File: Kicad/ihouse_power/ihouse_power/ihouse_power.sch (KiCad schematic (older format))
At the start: 14 parts, among them J10 Conn_02x07_Odd_Even, J11 Conn_01x06, J12 Conn_01x06, J14 Optic, J15 Hum1, J16 Hum2, J17 Hum3, J18 Temp, J19 I2C, J5 Conn_01x16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

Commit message: schemos, pcb ruosimas
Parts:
- added M3: ev1527receiver_module, ev1527:EV1527_Receiver, symbol ev1527_receiver_module:ev1527receiver_module
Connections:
- wire segments 159 -> 167
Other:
- moved on the sheet: J10, J11, J12, J14, J15, J16, J17, J18, J19, J5, J6, J7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

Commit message: schemos ir pcb plokstes ruosimas
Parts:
- M3: symbol ev1527_receiver_module:ev1527receiver_module -> ihouse_power-rescue:ev1527receiver_module-ev1527_receiver_module
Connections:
- wire segments 167 -> 166
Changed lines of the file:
@@
 EESchema Schematic File Version 4
 LIBS:ihouse_power-cache
-EELAYER 26 0
+EELAYER 29 0
 EELAYER END
 $Descr A4 11693 8268
@@
 F32 "QCH_D2" O L 2750 1350 50
 F33 "QCH_D3" O L 2750 1250 50
+F34 "3VDC" O L 2750 1650 50
 $EndSheet
 Wire Wire Line
@@
 	4100 3400 4450 3400
 $Comp
-L ev1527_receiver_module:ev1527receiver_module M3
+L ihouse_power-rescue:ev1527receiver_module-ev1527_receiver_module M3
 U 1 1 5CAFFFFB
 P 1350 1450
@@
 Connection ~ 2300 2100
 Wire Wire Line
-	2400 1650 2400 1900
-Wire Wire Line
-	1650 1650 2400 1650
+	1650 1650 2750 1650
 Wire Bus Line
 	5550 950  5550 2050

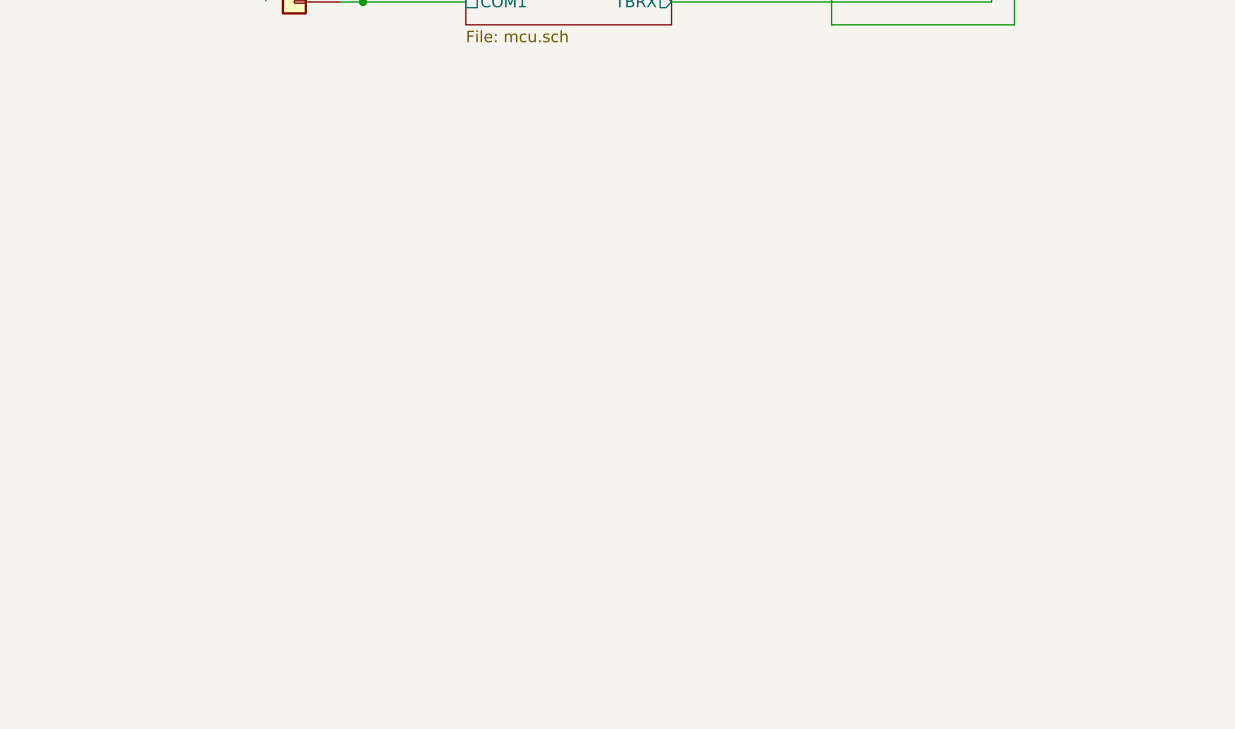
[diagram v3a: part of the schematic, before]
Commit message: prideta schema ir pcb lcd ekrano rs232 draiverio
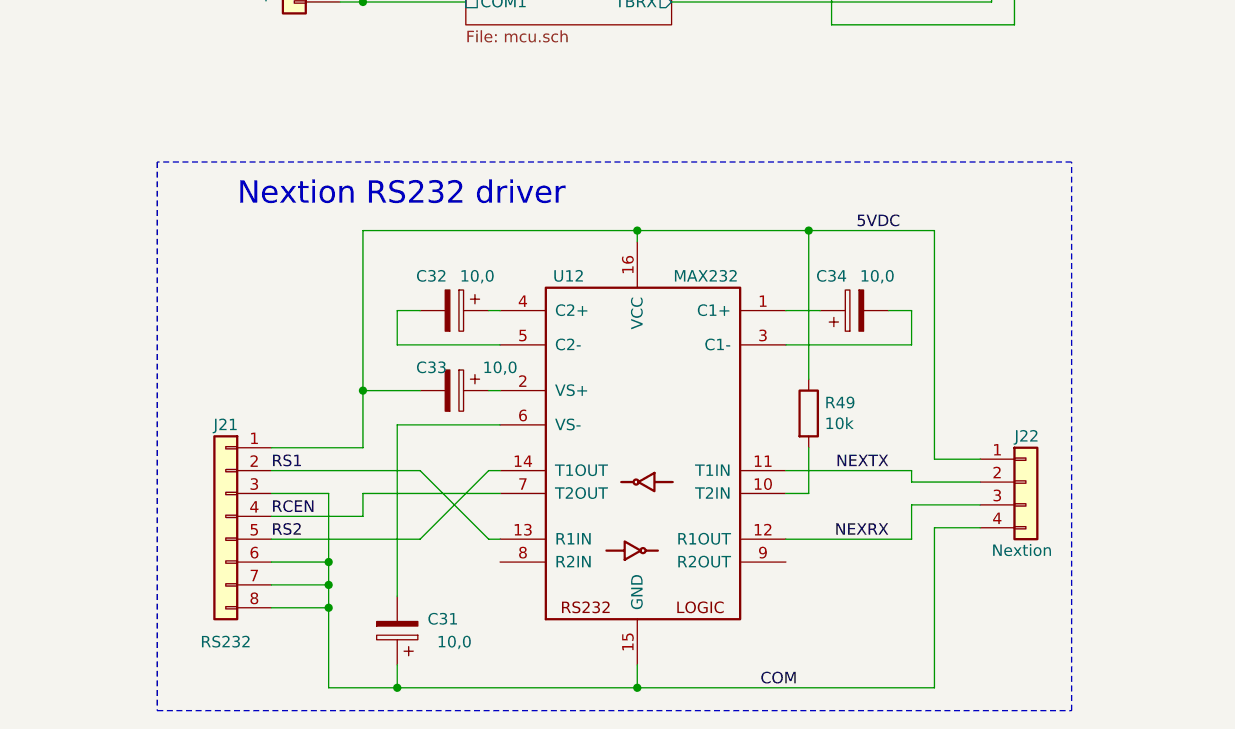
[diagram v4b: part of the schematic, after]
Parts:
- added C31, C32, C33, C34: 10,0, Capacitor_SMD:CP_Elec_3x5.4, symbol Device:CP
- added J21: RS232, Connector_PinHeader_2.54mm:PinHeader_1x08_P2.54mm_Horizontal, symbol Connector_Generic:Conn_01x08
- added J22: Nextion, Connector_PinHeader_2.54mm:PinHeader_1x04_P2.54mm_Vertical, symbol Connector_Generic:Conn_01x04
- added R49: 10k, symbol Device:R
- added U12: MAX232, Package_SO:SOIC-16_3.9x9.9mm_P1.27mm, symbol ihouse_power-rescue:MAX232-ics
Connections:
- new net: C34.1, U12.1 (C1+)
- new net: R49.2, U12.10 (T2IN)
- new net: C33.1, U12.2 (VS+)
- new net: C34.2, U12.3 (C1-)
- new net: C32.1, U12.4 (C2+)
- new net: C32.2, U12.5 (C2-)
- new net: C31.2, U12.6 (VS-)
- new net 5VDC: C33.2, J21.1 (Pin_1), J22.1 (Pin_1), R49.1, U12.16 (VCC)
- new net COM: C31.1, J21.3 (Pin_3), J21.6 (Pin_6), J21.7 (Pin_7), J21.8 (Pin_8), J22.4 (Pin_4), U12.15 (GND)
- new net NEXRX: J22.3 (Pin_3), U12.12 (R1OUT)
- new net NEXTX: J22.2 (Pin_2), U12.11 (T1IN)
- new net RCEN: J21.4 (Pin_4), U12.7 (T2OUT)
- new net RS1: J21.2 (Pin_2), U12.13 (R1IN)
- new net RS2: J21.5 (Pin_5), U12.14 (T1OUT)
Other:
- note added: "Nextion RS232 driver"
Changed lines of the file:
@@
 Wire Wire Line
 	1650 1650 2750 1650
+$Comp
+L ihouse_power-rescue:MAX232-ics U?
+U 1 1 5CF1CE1C
+P 3500 5900
+AR Path="/5D803411/5CF1CE1C" Ref="U?"  Part="1"
+AR Path="/5CF1CE1C" Ref="U12"  Part="1"
+F 0 "U12" H 3800 6700 50  0000 C CNN
+F 1 "MAX232" H 3200 6700 50  0000 C CNN
+F 2 "Package_SO:SOIC-16_3.9x9.9mm_P1.27mm" H 3550 4850 50  0001 L CNN
+F 3 "http://www.ti.com/lit/ds/symlink/max232.pdf" H 3500 5650 50  0001 C CNN
+	1    3500 5900
+	-1   0    0    -1
+$EndComp
+Wire Wire Line
+	3500 6800 3500 6900
+Text Label 4200 6900 2    50   ~ 0
+COM
+Wire Wire Line
+	2900 5250 2850 5250
+Wire Wire Line
+	2900 5400 2450 5400
+Wire Wire Line
+	2450 5400 2450 5250
+Wire Wire Line
+	2450 5250 2550 5250
+Wire Wire Line
+	4150 5250 4300 5250
+Wire Wire Line
+	4600 5250 4700 5250
+Wire Wire Line
+	4700 5250 4700 5400
+Wire Wire Line
+	4700 5400 4150 5400
+Wire Wire Line
+	2850 5600 2900 5600
+Wire Wire Line
+	3500 4900 2300 4900
+Wire Wire Line
+	2300 4900 2300 5600
+Wire Wire Line
+	3500 4900 3500 4950
+Wire Wire Line
+	2300 5600 2550 5600
+Wire Wire Line
+	2450 5750 2450 6500
+Wire Wire Line
+	2450 6800 2450 6900
+Wire Wire Line
+	2450 6900 3500 6900
+Connection ~ 3500 6900
+$Comp
+L Device:CP C?
+U 1 1 5CF1CE39
+P 2700 5250
+AR Path="/5D803411/5CF1CE39" Ref="C?"  Part="1"
+AR Path="/5CF1CE39" Ref="C32"  Part="1"
+F 0 "C32" V 2550 5150 50  0000 C CNN
+F 1 "10,0" V 2550 5350 50  0000 C CNN
+F 2 "Capacitor_SMD:CP_Elec_3x5.4" H 2738 5100 50  0001 C CNN
+F 3 "~" H 2700 5250 50  0001 C CNN
+	1    2700 5250
+	0    1    1    0
+$EndComp
+$Comp
+L Device:CP C?
+U 1 1 5CF1CE40
+P 4450 5250
+AR Path="/5D803411/5CF1CE40" Ref="C?"  Part="1"
+AR Path="/5CF1CE40" Ref="C34"  Part="1"
+F 0 "C34" V 4600 5350 50  0000 C CNN
+F 1 "10,0" V 4600 5150 50  0000 C CNN
+F 2 "Capacitor_SMD:CP_Elec_3x5.4" H 4488 5100 50  0001 C CNN
+F 3 "~" H 4450 5250 50  0001 C CNN
+	1    4450 5250
+	0    -1   -1   0
+$EndComp
+$Comp
+L Device:CP C?
+U 1 1 5CF1CE47
+P 2700 5600
+AR Path="/5D803411/5CF1CE47" Ref="C?"  Part="1"
+AR Path="/5CF1CE47" Ref="C33"  Part="1"
+F 0 "C33" V 2600 5500 50  0000 C CNN
+F 1 "10,0" V 2600 5800 50  0000 C CNN
+F 2 "Capacitor_SMD:CP_Elec_3x5.4" H 2738 5450 50  0001 C CNN
+F 3 "~" H 2700 5600 50  0001 C CNN
+	1    2700 5600
+	0    1    1    0
+$EndComp
+$Comp
+L Device:CP C?
+U 1 1 5CF1CE4E
+P 2450 6650
+AR Path="/5D803411/5CF1CE4E" Ref="C?"  Part="1"
+AR Path="/5CF1CE4E" Ref="C31"  Part="1"
+F 0 "C31" H 2250 6600 50  0000 C CNN
+F 1 "10,0" H 2200 6700 50  0000 C CNN
+F 2 "Capacitor_SMD:CP_Elec_3x5.4" H 2488 6500 50  0001 C CNN
+F 3 "~" H 2450 6650 50  0001 C CNN
+	1    2450 6650
+	-1   0    0    1
+$EndComp
+Wire Wire Line
+	2450 5750 2900 5750
+Wire Wire Line
+	1900 5850 2300 5850
+Wire Wire Line
+	2300 5850 2300 5600
+Connection ~ 2300 5600
+Wire Wire Line
+	1900 6350 2150 6350
+Wire Wire Line
+	2150 6350 2150 6450
+Wire Wire Line
+	2150 6550 1900 6550
+Wire Wire Line
+	1900 6450 2150 6450
+Connection ~ 2150 6450
+Wire Wire Line
+	2150 6450 2150 6550
+Wire Wire Line
+	1900 6250 2550 6250
+Wire Wire Line
+	1900 6050 2150 6050
+Wire Wire Line
+	2150 6050 2150 6350
+Connection ~ 2150 6350
+Wire Wire Line
+	1900 6150 2300 6150
+Wire Wire Line
+	2450 6900 2150 6900
+Wire Wire Line
+	2150 6900 2150 6550
+Connection ~ 2450 6900
+Connection ~ 2150 6550
+Text Label 4650 4900 2    50   ~ 0
+5VDC
+Wire Wire Line
+	3500 4900 4250 4900
+Connection ~ 3500 4900
+Wire Notes Line
+	1400 4600 1400 7000
+Wire Notes Line
+	1400 7000 5400 7000
+Wire Notes Line
+	5400 7000 5400 4600
+Wire Notes Line
+	5400 4600 1400 4600
+Text Notes 1750 4800 0    98   ~ 0
+Nextion RS232 driver
+Wire Wire Line
+	2550 6250 2850 5950
+Wire Wire Line
+	2850 5950 2900 5950
+Wire Wire Line
+	1900 5950 2550 5950
+Wire Wire Line
+	2550 5950 2850 6250
+Wire Wire Line
+	2850 6250 2900 6250
+Wire Wire Line
+	2900 6050 2300 6050
+Wire Wire Line
+	2300 6050 2300 6150
+$Comp
+L Device:R R49
+U 1 1 5D0DFE3F
+P 4250 5700
+F 0 "R49" H 4320 5746 50  0000 L CNN
+F 1 "10k" H 4320 5655 50  0000 L CNN
+F 2 "" V 4180 5700 50  0001 C CNN
+F 3 "~" H 4250 5700 50  0001 C CNN
+	1    4250 5700
+	1    0    0    -1
+$EndComp
+Wire Wire Line
+	4150 6050 4250 6050
+Wire Wire Line
+	4250 6050 4250 5850
+Wire Wire Line
+	4250 5550 4250 4900
+Connection ~ 4250 4900
+Text Label 4600 5950 2    50   ~ 0
+NEXTX
+Text Label 4600 6250 2    50   ~ 0
+NEXRX
+Text Label 1900 5950 0    50   ~ 0
+RS1
+Text Label 1900 6250 0    50   ~ 0
+RS2
+$Comp
+L Connector_Generic:Conn_01x08 J21
+U 1 1 5D1D3B9A
+P 1700 6150
+F 0 "J21" H 1700 6550 50  0000 C CNN
+F 1 "RS232" H 1700 5600 50  0000 C CNN
+F 2 "Connector_PinHeader_2.54mm:PinHeader_1x08_P2.54mm_Horizontal" H 1700 6150 50  0001 C CNN
+F 3 "~" H 1700 6150 50  0001 C CNN
+	1    1700 6150
+	-1   0    0    -1
+$EndComp
+Text Label 1900 6150 0    50   ~ 0
+RCEN
+$Comp
+L Connector_Generic:Conn_01x04 J22
+U 1 1 5D21FC01
+P 5200 6000
+F 0 "J22" H 5150 6200 50  0000 L CNN
+F 1 "Nextion" H 5050 5700 50  0000 L CNN
+F 2 "Connector_PinHeader_2.54mm:PinHeader_1x04_P2.54mm_Vertical" H 5200 6000 50  0001 C CNN
+F 3 "~" H 5200 6000 50  0001 C CNN
+	1    5200 6000
+	1    0    0    -1
+$EndComp
+Wire Wire Line
+	4800 4900 4800 5900
+Wire Wire Line
+	4800 5900 5000 5900
+Wire Wire Line
+	4250 4900 4800 4900
+Wire Wire Line
+	4800 6900 4800 6200
+Wire Wire Line
+	4800 6200 5000 6200
+Wire Wire Line
+	3500 6900 4800 6900
+Wire Wire Line
+	4700 6250 4700 6100
+Wire Wire Line
+	4700 6100 5000 6100
+Wire Wire Line
+	4150 6250 4700 6250
+Wire Wire Line
+	4700 5950 4700 6000
+Wire Wire Line
+	4700 6000 5000 6000
+Wire Wire Line
+	4150 5950 4700 5950
 Wire Bus Line
 	5550 950  5550 2050

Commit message: tarpinis komitas
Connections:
- net NEXRX: now also J22.2 (Pin_2); no longer J22.3 (Pin_3)
- net NEXTX: now also J22.3 (Pin_3); no longer J22.2 (Pin_2)
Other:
- moved on the sheet: C31, C32, C33, C34, J21, J22, R49, U12

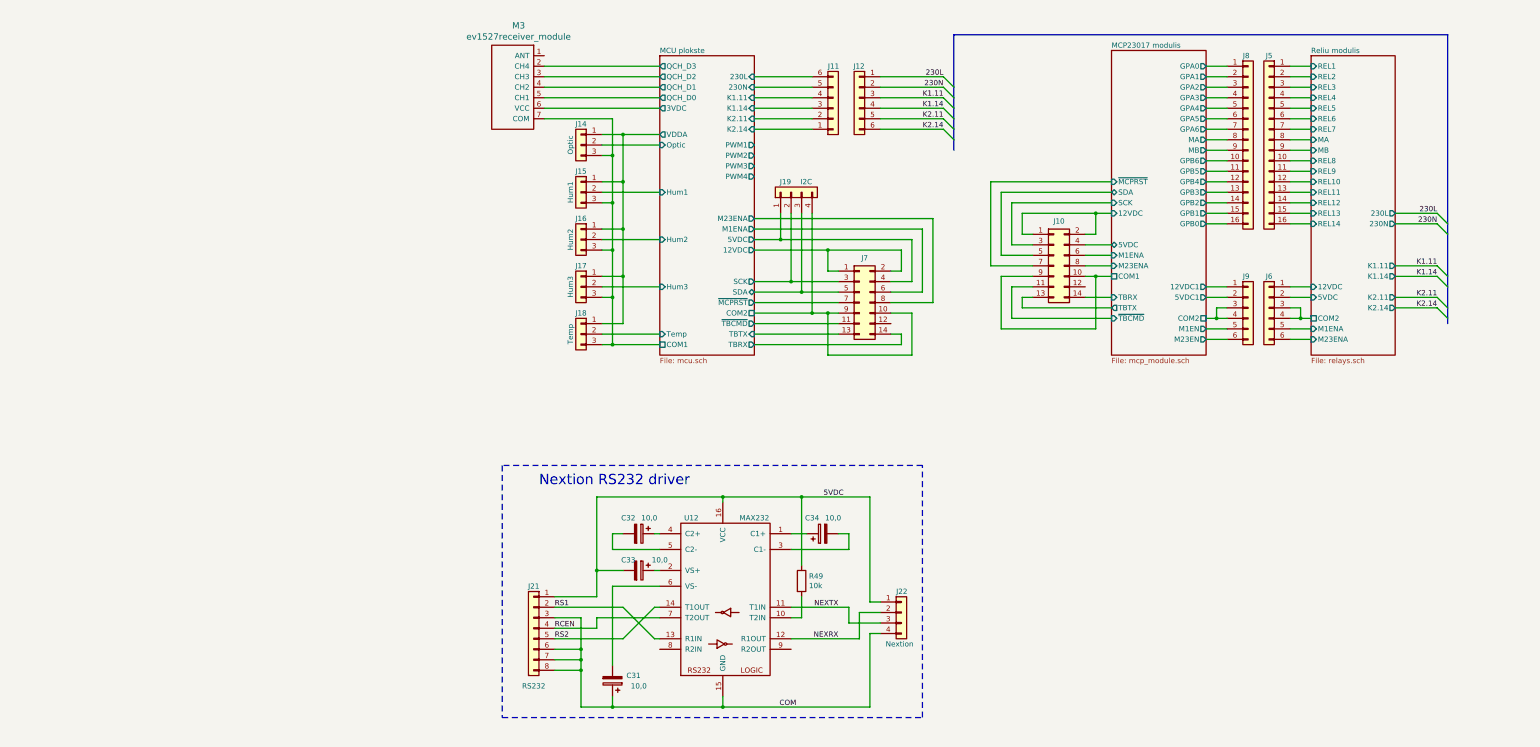
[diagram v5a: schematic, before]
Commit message: nupiesta paskirstymo dezutes schema ir pcb
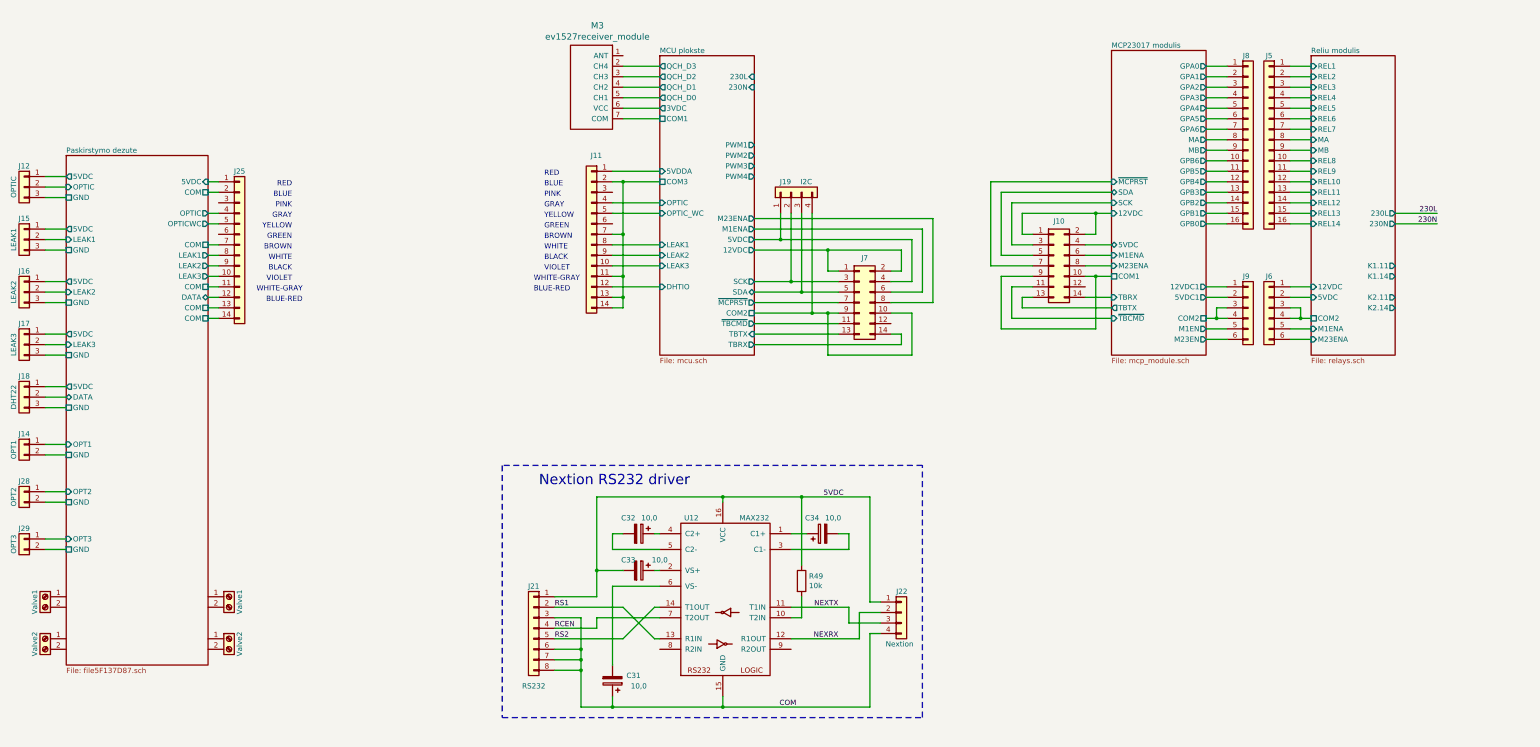
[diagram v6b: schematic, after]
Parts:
- removed J11: Conn_01x06, Connector_PinHeader_2.54mm:PinHeader_1x06_P2.54mm_Vertical, symbol Connector_Generic:Conn_01x06
- removed J12: Conn_01x06, symbol Connector_Generic:Conn_01x06
- removed J14: Optic, Connector_JST:JST_PH_B3B-PH-K_1x03_P2.00mm_Vertical, symbol Connector_Generic:Conn_01x03
- removed J15: Hum1, Connector_JST:JST_PH_B3B-PH-K_1x03_P2.00mm_Vertical, symbol Connector_Generic:Conn_01x03
- removed J16: Hum2, Connector_JST:JST_PH_B3B-PH-K_1x03_P2.00mm_Vertical, symbol Connector_Generic:Conn_01x03
- removed J17: Hum3, Connector_JST:JST_PH_B3B-PH-K_1x03_P2.00mm_Vertical, symbol Connector_Generic:Conn_01x03
- removed J18: Temp, Connector_JST:JST_PH_B3B-PH-K_1x03_P2.00mm_Vertical, symbol Connector_Generic:Conn_01x03
- added J11, J507: Conn_01x14, symbol Connector_Generic:Conn_01x14
- added J30: OPT3, symbol Connector_Generic:Conn_01x02
- added J500: OPTIC, symbol Connector_Generic:Conn_01x03
- added J502: LEAK1, symbol Connector_Generic:Conn_01x03
- added J503: LEAK2, symbol Connector_Generic:Conn_01x03
- added J504: LEAK3, symbol Connector_Generic:Conn_01x03
- added J505: DHT22, symbol Connector_Generic:Conn_01x03
- added J506, J508: Valve1, symbol Connector:Screw_Terminal_01x02
- added J509, J510: Valve2, symbol Connector:Screw_Terminal_01x02
- added J511: OPT2, symbol Connector_Generic:Conn_01x02
- added J512: OPT1, symbol Connector_Generic:Conn_01x02
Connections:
- new net MCU plokste/5VDDA: J11.1 (Pin_1)
- new net MCU plokste/COM3: J11.11 (Pin_11), J11.13 (Pin_13), J11.14 (Pin_14), J11.2 (Pin_2), J11.7 (Pin_7)
- new net MCU plokste/DHTIO: J11.12 (Pin_12)
- new net MCU plokste/LEAK1: J11.8 (Pin_8)
- new net MCU plokste/LEAK2: J11.9 (Pin_9)
- new net MCU plokste/LEAK3: J11.10 (Pin_10)
- new net MCU plokste/OPTIC: J11.4 (Pin_4)
- new net MCU plokste/OPTIC_WC: J11.5 (Pin_5)
- new net Paskirstymo dezute/5VDC: J507.1 (Pin_1)
- new net Paskirstymo dezute/5VDC: J500.1 (Pin_1)
- new net Paskirstymo dezute/5VDC: J502.1 (Pin_1)
- new net Paskirstymo dezute/5VDC: J503.1 (Pin_1)
- new net Paskirstymo dezute/5VDC: J504.1 (Pin_1)
- new net Paskirstymo dezute/5VDC: J505.1 (Pin_1)
- new net Paskirstymo dezute/COM: J507.11 (Pin_11)
- new net Paskirstymo dezute/COM: J507.13 (Pin_13)
- new net Paskirstymo dezute/COM: J507.14 (Pin_14)
- new net Paskirstymo dezute/COM: J507.2 (Pin_2)
- new net Paskirstymo dezute/COM: J507.7 (Pin_7)
- new net Paskirstymo dezute/DATA: J507.12 (Pin_12)
- new net Paskirstymo dezute/DATA: J505.2 (Pin_2)
- new net Paskirstymo dezute/GND: J512.2 (Pin_2)
- new net Paskirstymo dezute/GND: J511.2 (Pin_2)
- new net Paskirstymo dezute/GND: J30.2 (Pin_2)
- new net Paskirstymo dezute/GND: J500.3 (Pin_3)
- new net Paskirstymo dezute/GND: J502.3 (Pin_3)
- new net Paskirstymo dezute/GND: J503.3 (Pin_3)
- new net Paskirstymo dezute/GND: J504.3 (Pin_3)
- new net Paskirstymo dezute/GND: J505.3 (Pin_3)
- new net Paskirstymo dezute/LEAK1: J507.8 (Pin_8)
- new net Paskirstymo dezute/LEAK1: J502.2 (Pin_2)
- new net Paskirstymo dezute/LEAK2: J507.9 (Pin_9)
- new net Paskirstymo dezute/LEAK2: J503.2 (Pin_2)
- new net Paskirstymo dezute/LEAK3: J507.10 (Pin_10)
- new net Paskirstymo dezute/LEAK3: J504.2 (Pin_2)
- new net Paskirstymo dezute/OPT1: J512.1 (Pin_1)
- new net Paskirstymo dezute/OPT2: J511.1 (Pin_1)
- new net Paskirstymo dezute/OPT3: J30.1 (Pin_1)
- new net Paskirstymo dezute/OPTIC: J507.4 (Pin_4)
- new net Paskirstymo dezute/OPTIC: J500.2 (Pin_2)
- new net Paskirstymo dezute/OPTICWC: J507.5 (Pin_5)
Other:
- note added: "BLACK"
- note added: "BLUE"
- note added: "BLUE-RED"
- note added: "BROWN"
- note added: "GRAY"
- note added: "GREEN"
- note added: "PINK"
- note added: "RED"
- note added: "VIOLET"
- note added: "WHITE"
- note added: "WHITE-GRAY"
- note added: "YELLOW"
- moved on the sheet: M3
